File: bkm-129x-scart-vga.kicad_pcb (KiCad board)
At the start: 2 copper layers, 105 x 160 mm, 66 parts, among them J1 DB15_Female_HighDensity_Mount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, J2 SCART-F, J3 SJ1-353XNG, J5 Conn_02x32_Row_Letter_Last, J6 ICSP, Q1 DTC144EKA, Q2 MMBT3904, SW1 PBH4UEENAGX, SW2 PBH4UEENAGX, U1 ADG1611, U101 LDL1117S50R, U2 THS7374, U4 74LVC125, U5 MIC3490-5.0, U6 ATMEGA328PB-AU, Y1 CSTNE16M0VH3L000R0

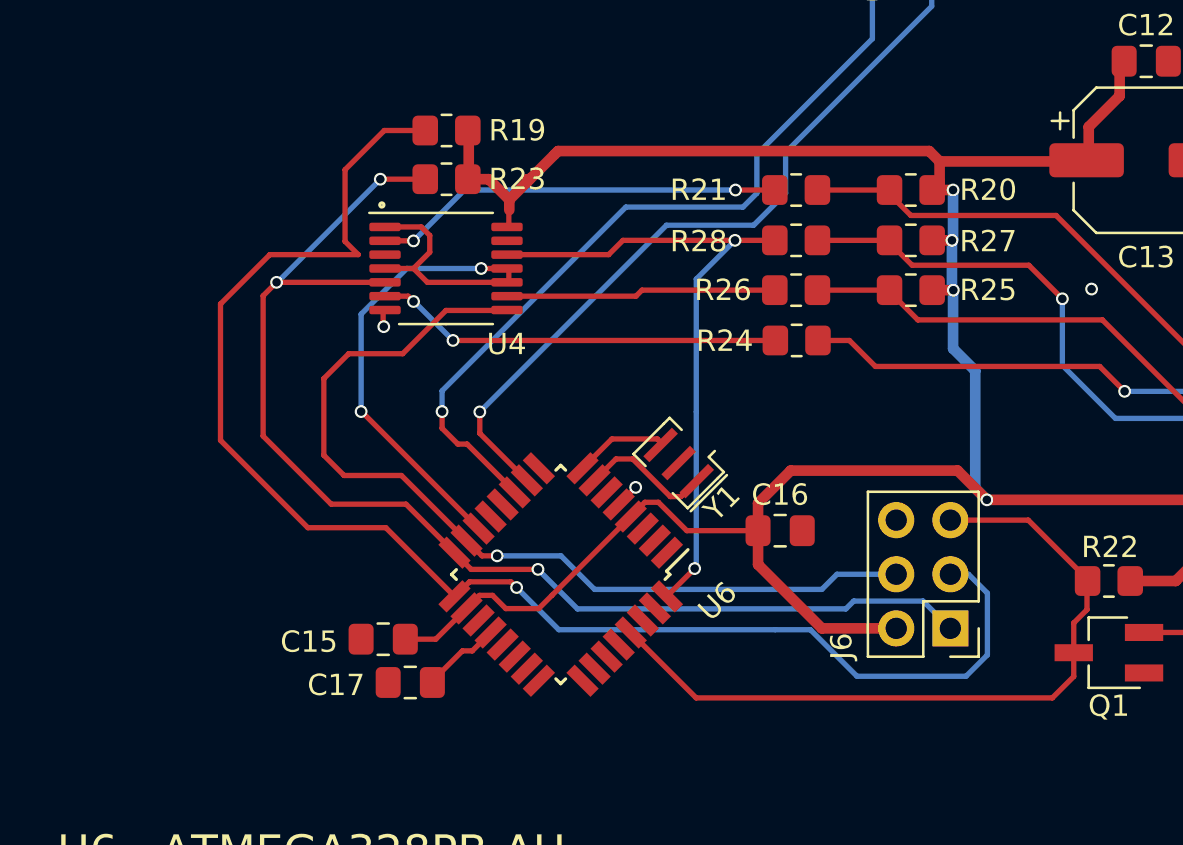
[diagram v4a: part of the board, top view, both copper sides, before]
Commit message: Update PCB from schematic, arrange MCU components on PCB.
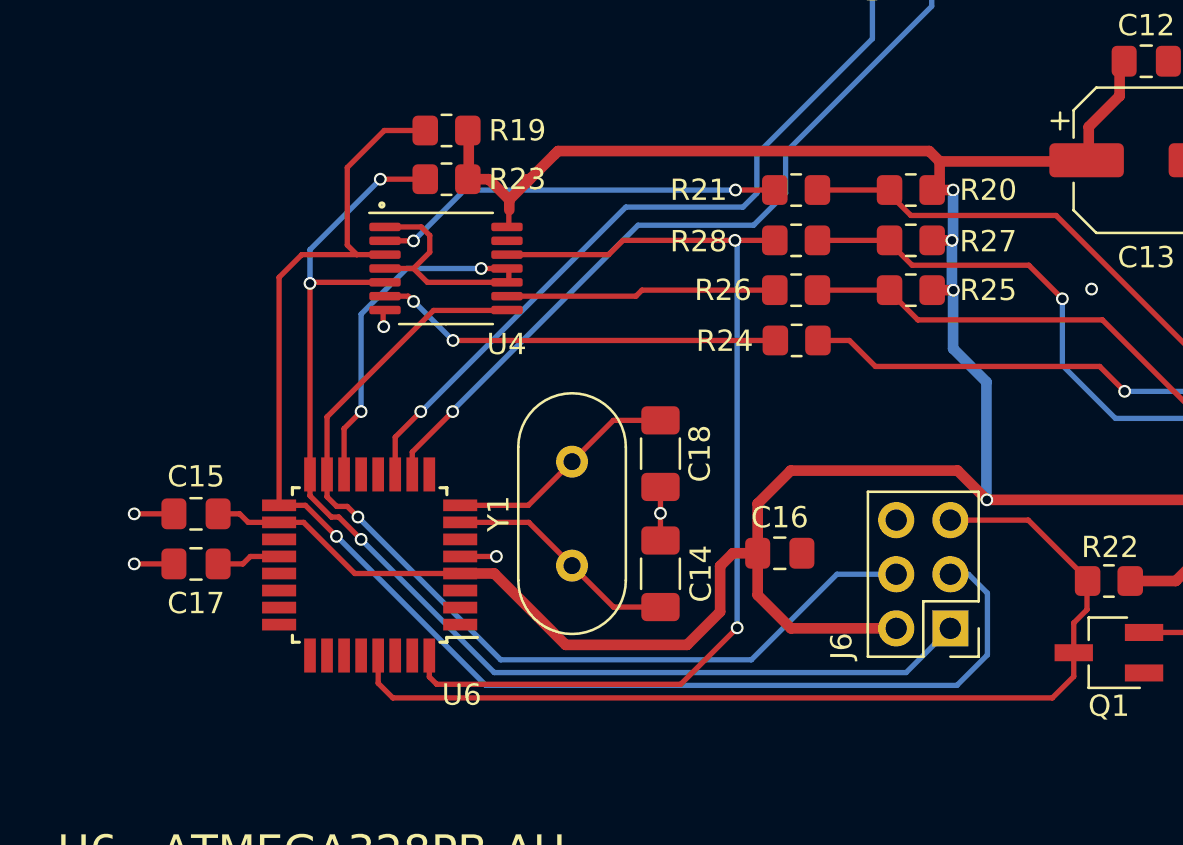
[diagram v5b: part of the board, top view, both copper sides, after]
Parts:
- added C14: 22pF, Capacitor_SMD:C_1206_3216Metric_Pad1.33x1.80mm_HandSolder, F.Cu at (110.6, 140.3)
- added C18: 22pF, Capacitor_SMD:C_1206_3216Metric_Pad1.33x1.80mm_HandSolder, F.Cu at (110.6, 134.7)
- Y1: value CSTNE16M0VH3L000R0 -> 16MHz; footprint Crystal:Resonator_SMD_muRata_CSTxExxV-3Pin_3.0x1.1mm -> Crystal:Crystal_HC49-U_Vertical
- moved C17 11.5 mm to (88.8, 139.8)
- moved C15 10.6 mm to (88.8, 137.5)
- moved U6 8.98 mm to (97.0, 139.9), turned to 180 degrees
- moved Y1 5.01 mm to (106.5, 135.1), turned to -90 degrees
- moved C16 1.06 mm to (116.2, 139.3)
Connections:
- net /P-B/B renamed /P-B/B
- net /P-R/R renamed /P-R/R
- net /Y/G renamed /Y/G
- net VDD renamed VDDA
- net VSS renamed VSSA
- C10 pad 2: GND -> GNDA
- C101 pad 2: GND -> GNDA
- C102 pad 2: GND -> GNDA
- C11 pad 1: GND -> GNDA
- C12 pad 2: GND -> GNDA
- C13 pad 2: GND -> GNDA
- C15 pad 2: GND -> GNDA
- C16 pad 2: GND -> GNDA
- C17 pad 1: GND -> GNDA
- C5 pad 2: GND -> GNDA
- C6 pad 2: GND -> GNDA
- C7 pad 2: GND -> GNDA
- C8 pad 1: GND -> GNDA
- C9 pad 2: GND -> GNDA
- J1 pad 0: GND -> GNDA
- J1 pad 10: GND -> GNDA
- J1 pad 11: (no net) -> unconnected-(J1-Pad11)
- J1 pad 12: (no net) -> unconnected-(J1-Pad12)
- J1 pad 15: (no net) -> unconnected-(J1-Pad15)
- J1 pad 4: (no net) -> unconnected-(J1-Pad4)
- J1 pad 5: GND -> GNDA
- J1 pad 6: GND -> GNDA
- J1 pad 7: GND -> GNDA
- J1 pad 8: GND -> GNDA
- J1 pad 9: (no net) -> unconnected-(J1-Pad9)
- J2 pad 1: (no net) -> unconnected-(J2-P1-Pad1)
- J2 pad 10: (no net) -> unconnected-(J2-P10-Pad10)
- J2 pad 12: (no net) -> unconnected-(J2-P12-Pad12)
- J2 pad 13: GND -> GNDA
- J2 pad 14: (no net) -> unconnected-(J2-P14-Pad14)
- J2 pad 16: (no net) -> unconnected-(J2-P16-Pad16)
- J2 pad 17: GND -> GNDA
- J2 pad 18: GND -> GNDA
- J2 pad 19: (no net) -> unconnected-(J2-P19-Pad19)
- J2 pad 21: GND -> GNDA
- J2 pad 3: (no net) -> unconnected-(J2-P3-Pad3)
- J2 pad 4: GND -> GNDA
- J2 pad 5: GND -> GNDA
- J2 pad 8: (no net) -> unconnected-(J2-P8-Pad8)
- J2 pad 9: GND -> GNDA
- J3 pad 3: GND -> GNDA
- J3 pad 4: (no net) -> unconnected-(J3-Pad4)
- J3 pad 5: (no net) -> unconnected-(J3-Pad5)
- J5 pad 10a: GND -> GNDA
- J5 pad 10b: (no net) -> unconnected-(J5-Pin_10b-Pad10b)
- J5 pad 11a: GND -> GNDA
- J5 pad 12a: GND -> GNDA
- J5 pad 13a: GND -> GNDA
- J5 pad 14a: GND -> GNDA
- J5 pad 15a: GND -> GNDA
- J5 pad 16a: GND -> GNDA
- J5 pad 17a: (no net) -> unconnected-(J5-Pin_17a-Pad17a)
- J5 pad 17b: GND -> GNDA
- J5 pad 18a: (no net) -> unconnected-(J5-Pin_18a-Pad18a)
- J5 pad 18b: (no net) -> unconnected-(J5-Pin_18b-Pad18b)
- J5 pad 19a: (no net) -> unconnected-(J5-Pin_19a-Pad19a)
- J5 pad 19b: (no net) -> unconnected-(J5-Pin_19b-Pad19b)
- J5 pad 1a: GND -> GNDA
- J5 pad 1b: GND -> GNDA
- J5 pad 23a: GND -> GNDA
- J5 pad 23b: (no net) -> unconnected-(J5-Pin_23b-Pad23b)
- J5 pad 24a: GND -> GNDA
- J5 pad 24b: (no net) -> unconnected-(J5-Pin_24b-Pad24b)
- J5 pad 25a: (no net) -> unconnected-(J5-Pin_25a-Pad25a)
- J5 pad 25b: (no net) -> unconnected-(J5-Pin_25b-Pad25b)
- J5 pad 26a: (no net) -> unconnected-(J5-Pin_26a-Pad26a)
- J5 pad 27a: (no net) -> unconnected-(J5-Pin_27a-Pad27a)
- J5 pad 2a: (no net) -> unconnected-(J5-Pin_2a-Pad2a)
- J5 pad 2b: (no net) -> unconnected-(J5-Pin_2b-Pad2b)
- J5 pad 30a: GND -> GNDA
- J5 pad 30b: GND -> GNDA
- J5 pad 31b: (no net) -> unconnected-(J5-Pin_31b-Pad31b)
- J5 pad 32a: GND -> GNDA
- J5 pad 32b: GND -> GNDA
- J5 pad 3a: GND -> GNDA
- J5 pad 3b: GND -> GNDA
- J5 pad 4a: (no net) -> unconnected-(J5-Pin_4a-Pad4a)
- J5 pad 4b: (no net) -> unconnected-(J5-Pin_4b-Pad4b)
- J5 pad 5a: (no net) -> unconnected-(J5-Pin_5a-Pad5a)
- J5 pad 5b: (no net) -> unconnected-(J5-Pin_5b-Pad5b)
- J5 pad 8a: GND -> GNDA
- J5 pad 8b: (no net) -> unconnected-(J5-Pin_8b-Pad8b)
- J5 pad 9a: GND -> GNDA
- J5 pad 9b: (no net) -> unconnected-(J5-Pin_9b-Pad9b)
- J6 pad 6: GND -> GNDA
- Q1 pad 1: GND -> GNDA
- R10 pad 2: GND -> GNDA
- R11 pad 2: GND -> GNDA
- R12 pad 2: GND -> GNDA
- R13 pad 2: GND -> GNDA
- R14 pad 1: GND -> GNDA
- R32 pad 2: GND -> GNDA
- R33 pad 2: GND -> GNDA
- R34 pad 2: GND -> GNDA
- R5 pad 1: GND -> GNDA
- SW1 pad 1: GND -> GNDA
- SW1 pad 5: GND -> GNDA
- U1 pad 5: GND -> GNDA
- U101 pad 1: GND -> GNDA
- U2 pad 5: GND -> GNDA
- U2 pad 6: GND -> GNDA
- U2 pad 7: (no net) -> unconnected-(U2-NC-Pad7)
- U2 pad 8: (no net) -> unconnected-(U2-NC-Pad8)
- U4 pad 13: GND -> GNDA
- U4 pad 7: GND -> GNDA
- U5 pad 1: (no net) -> unconnected-(U5-NC-Pad1)
- U5 pad 2: GND -> GNDA
- U6 pad 1: (no net) -> unconnected-(U6-(OC2B/INT1/PTCXY)PD3-Pad1)
- U6 pad 12: (no net) -> unconnected-(U6-(CLKO/ICP1/PTCXY)PB0-Pad12)
- U6 pad 13: (no net) -> unconnected-(U6-(OC1A/PTCXY)PB1-Pad13)
- U6 pad 19: (no net) -> unconnected-(U6-PE2(PTCY/ADC6/ICP3/~{SS1})-Pad19)
- U6 pad 2: (no net) -> unconnected-(U6-(XCK0/T0/PTCXY)PD4-Pad2)
- U6 pad 21: GND -> GNDA
- U6 pad 22: (no net) -> unconnected-(U6-PE3(PTCY/ADC7/T3/MOSI1)-Pad22)
- U6 pad 23: (no net) -> unconnected-(U6-(MISO1/ADC0/PTCY)PC0-Pad23)
- U6 pad 24: (no net) -> unconnected-(U6-(SCK1/ADC1/PTCY)PC1-Pad24)
- U6 pad 25: (no net) -> unconnected-(U6-(ADC2/PTCY)PC2-Pad25)
- U6 pad 26: (no net) -> unconnected-(U6-(ADC3/PTCY)PC3-Pad26)
- U6 pad 27: (no net) -> unconnected-(U6-(SDA0/ADC4/PTCY)PC4-Pad27)
- U6 pad 28: (no net) -> unconnected-(U6-(SCL0/ADC5/PTCY)PC5-Pad28)
- U6 pad 3: (no net) -> unconnected-(U6-PE0(PTCXY/SDA1/ICP4/ACO)-Pad3)
- U6 pad 30: (no net) -> unconnected-(U6-(RXD0/OC3A/PTCXY)PD0-Pad30)
- U6 pad 31: (no net) -> unconnected-(U6-(TXD0/OC4A/PTCXY)PD1-Pad31)
- U6 pad 5: GND -> GNDA
- U6 pad 6: (no net) -> unconnected-(U6-PE1(PTCXY/SCL1/T4)-Pad6)
- U6 pad 7: Net-(U6-Pad7) -> Net-(U6-(XTAL1/TOSC1)PB6)
- U6 pad 8: Net-(U6-Pad8) -> Net-(U6-(XTAL2/TOSC2)PB7)
- U6 pad 9: (no net) -> unconnected-(U6-(OC0B/T1/PTCXY)PD5-Pad9)
- Y1 pad 1: Net-(U6-Pad7) -> Net-(U6-(XTAL2/TOSC2)PB7)
- Y1 pad 2: GND -> Net-(U6-(XTAL1/TOSC1)PB6)
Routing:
- net GNDA: track 0.00 -> 20.5 mm, vias 0 -> 17
- net MCU_SLOT_ID: track 30.5 -> 47.4 mm
- net GND: track 13.7 -> 0.00 mm, vias 14 -> 0
- net ~{MCU_RESET}: track 34.9 -> 47.0 mm
- net +5VD: track 126.3 -> 138.0 mm
- net Net-(U6-(XTAL2/TOSC2)PB7): track 0.00 -> 11.1 mm
- net Net-(U6-(XTAL1/TOSC1)PB6): track 0.00 -> 11.0 mm
- net Net-(U6-Pad7): track 6.41 -> 0.00 mm
- net ~{MCU_SS}: track 31.2 -> 26.7 mm
- net Net-(U6-Pad8): track 4.37 -> 0.00 mm
- net MCU_MOSI: track 43.4 -> 45.9 mm
- net MCU_SCK: track 68.8 -> 66.8 mm
- net MCU_MISO: track 57.4 -> 55.8 mm
- net ~{EXT_SYNC_OE}: track 42.8 -> 41.2 mm
- net ~{BX_OE}: track 53.6 -> 54.6 mm
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- added copper zone on B.Cu, net GNDA
- added copper zone on F.Cu, net GNDA
- removed copper zone on B.Cu, net GND
- removed copper zone on F.Cu, net GND

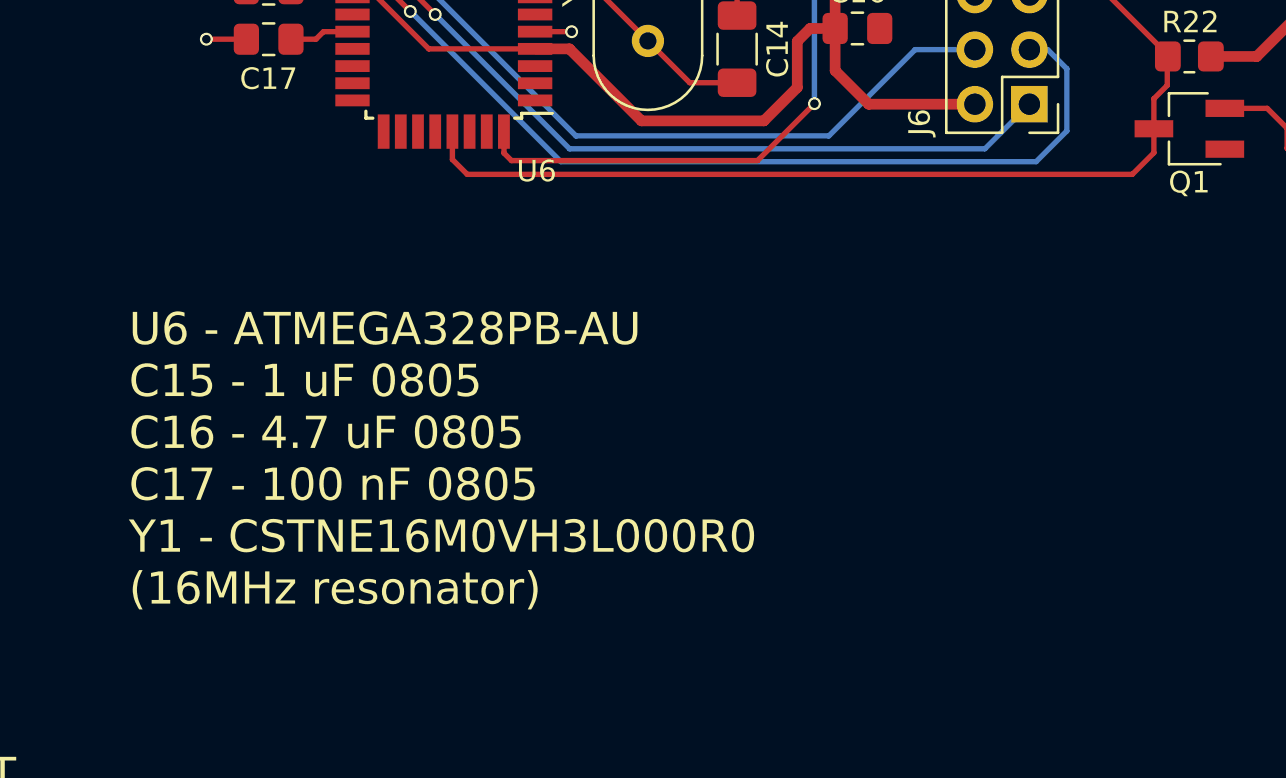
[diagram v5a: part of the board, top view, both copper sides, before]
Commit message: Add debug UART connector to schematic and PCB. Edit silkscreen MCU description.
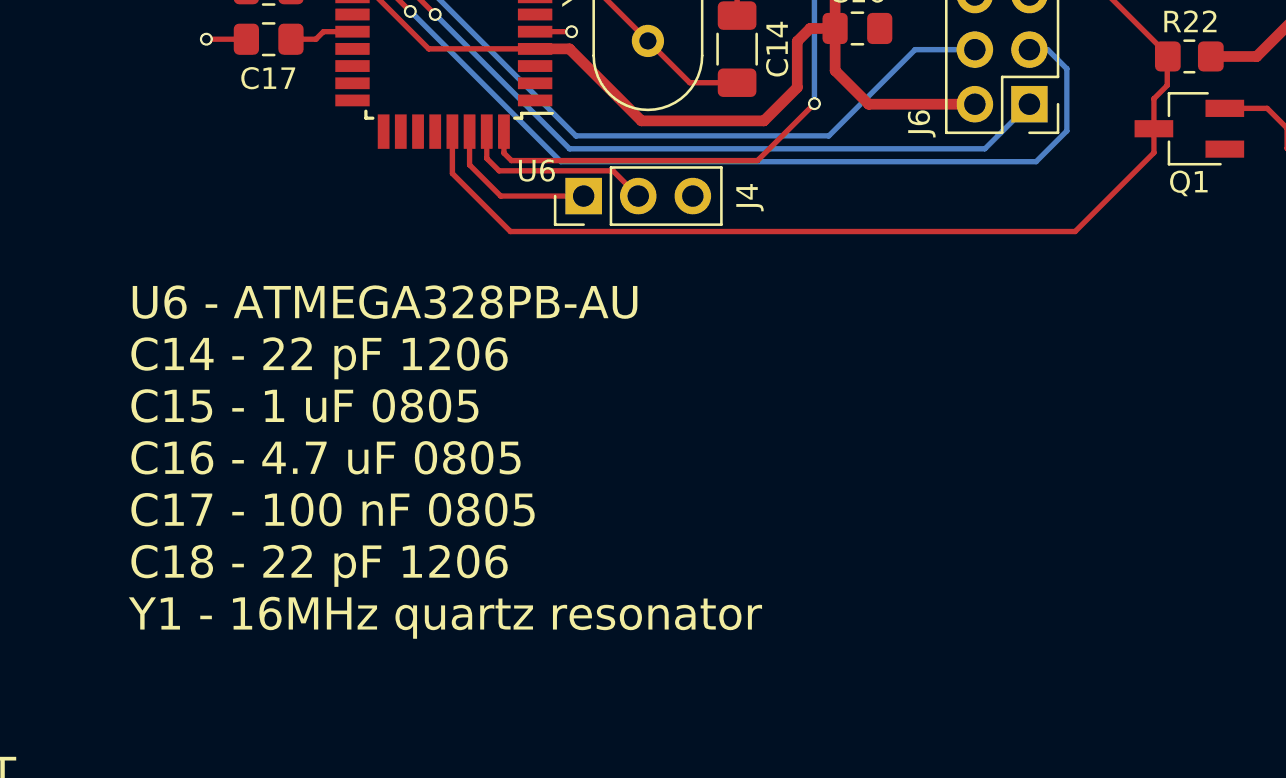
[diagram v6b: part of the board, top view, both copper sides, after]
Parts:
- added J4: UART, Connector_PinHeader_2.54mm:PinHeader_1x03_P2.54mm_Vertical, F.Cu at (103.5, 147.2)
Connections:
- U6 pad 30: unconnected-(U6-(RXD0/OC3A/PTCXY)PD0-Pad30) -> MCU_RX
- U6 pad 31: unconnected-(U6-(TXD0/OC4A/PTCXY)PD1-Pad31) -> MCU_TX
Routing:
- net MCU_TX: track 0.00 -> 9.02 mm
- net MCU_RX: track 0.00 -> 7.46 mm
- net ~{MCU_RESET}: track 47.0 -> 49.6 mm
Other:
- board text added: "U6 - ATMEGA328PB-AU C14 - 22 pF 1206 C15 - 1 uF 0805 C16 - 4.7 uF 0805 C17 - 100 nF 0805 C18 - 22 pF 1206 Y1 - 16MHz quartz resonator"
- board text removed: "U6 - ATMEGA328PB-AU C15 - 1 uF 0805 C16 - 4.7 uF 0805 C17 - 100 nF 0805 Y1 - CSTNE16M0VH3L000R0 (16MHz resonator)"
